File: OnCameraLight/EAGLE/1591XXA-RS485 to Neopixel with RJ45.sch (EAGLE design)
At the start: 16 parts, among them IC1 75176AP, J1 RJHSE-5381

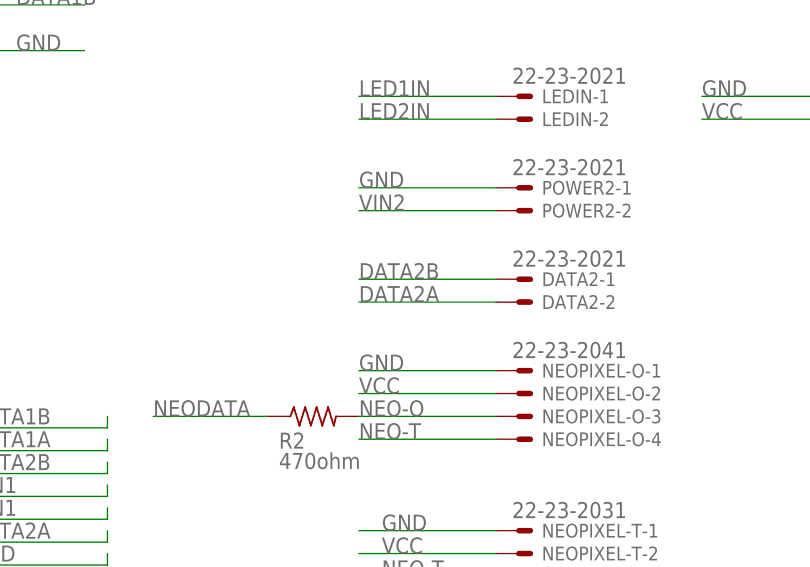
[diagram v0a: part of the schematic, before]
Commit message: Go through and fix notation on RS485 wiring everywhere to use the standard A/B notation.
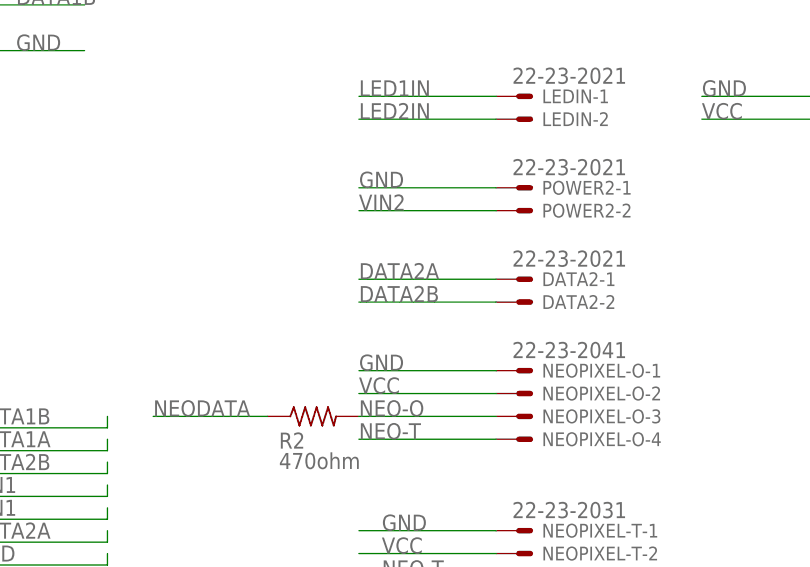
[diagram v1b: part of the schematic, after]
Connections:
- net DATA2A: now also DATA2-1.S; no longer DATA2-2.S
- net DATA2B: now also DATA2-2.S; no longer DATA2-1.S
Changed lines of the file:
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@@
 </segment>
 <segment>
-<pinref part="DATA2" gate="-1" pin="S"/>
-<wire x1="149.86" y1="104.14" x2="134.62" y2="104.14" width="0.1524" layer="91"/>
-<label x="134.62" y="104.14" size="1.778" layer="95"/>
+<pinref part="DATA2" gate="-2" pin="S"/>
+<wire x1="149.86" y1="101.6" x2="134.62" y2="101.6" width="0.1524" layer="91"/>
+<label x="134.62" y="101.6" size="1.778" layer="95"/>
 </segment>
 </net>
@@
 </segment>
 <segment>
-<pinref part="DATA2" gate="-2" pin="S"/>
-<wire x1="149.86" y1="101.6" x2="134.62" y2="101.6" width="0.1524" layer="91"/>
-<label x="134.62" y="101.6" size="1.778" layer="95"/>
+<pinref part="DATA2" gate="-1" pin="S"/>
+<wire x1="149.86" y1="104.14" x2="134.62" y2="104.14" width="0.1524" layer="91"/>
+<label x="134.62" y="104.14" size="1.778" layer="95"/>
 </segment>
 </net>
